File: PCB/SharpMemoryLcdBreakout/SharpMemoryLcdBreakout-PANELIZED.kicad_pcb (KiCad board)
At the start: 2 copper layers, 62 x 42 mm, 49 parts, among them J1 Pin Header, J2 EMD, J3 FH12-10S-0.5SH

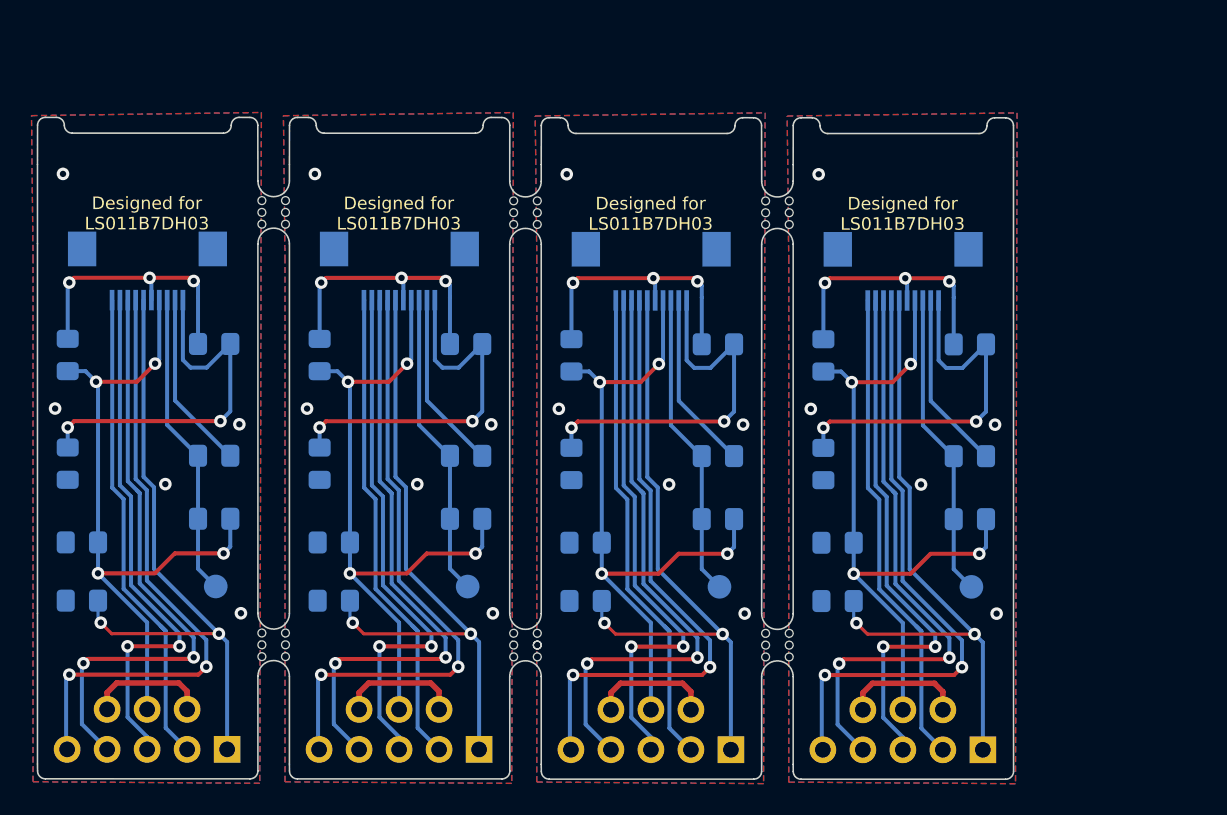
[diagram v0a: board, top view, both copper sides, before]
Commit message: going back to 0603 for easier part selection
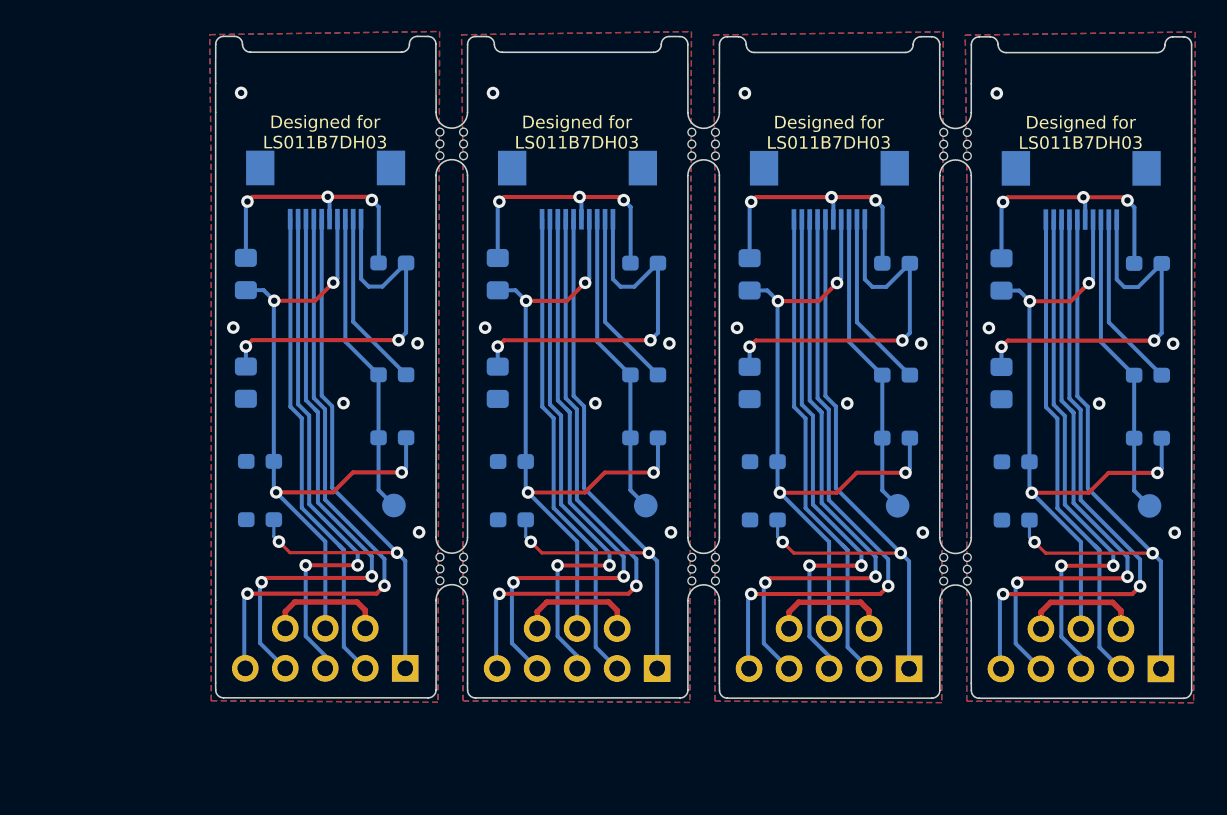
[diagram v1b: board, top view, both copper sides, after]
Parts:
- removed ? (x3): , 
- removed the C1 at (89.4, 67.3)
- removed the C1 at (73.4, 67.3)
- removed the C1 at (57.4, 67.3)
- removed the C2 at (81.8, 51.0)
- removed the C2 at (97.8, 51.0)
- removed the C2 at (65.8, 51.0)
- removed the C3 at (89.4, 63.6)
- removed the C3 at (57.4, 63.6)
- removed the C3 at (73.4, 63.6)
- removed the FB1 at (56.5, 51.7)
- removed the FB1 at (72.5, 51.7)
- removed the FB1 at (88.5, 51.7)
- removed the FB2 at (72.5, 58.6)
- removed the FB2 at (56.5, 58.6)
- removed the FB2 at (88.5, 58.6)
- removed the J1 at (82.6, 76.7)
- removed the J1 at (98.6, 76.7)
- removed the J1 at (66.6, 76.7)
- removed the J2 at (81.9, 66.4)
- removed the J2 at (65.9, 66.4)
- removed the J2 at (97.9, 66.4)
- removed the J3 at (93.6, 46.4)
- removed the J3 at (61.6, 46.3)
- removed the J3 at (77.6, 46.3)
- removed the R1 at (97.8, 58.1)
- removed the R1 at (65.8, 58.1)
- removed the R1 at (81.8, 58.1)
- removed the R2 at (81.8, 62.1)
- removed the R2 at (65.8, 62.1)
- removed the R2 at (97.8, 62.1)
- removed the mouse-bite-2mm-slot at (85.6, 70.1)
- removed the mouse-bite-2mm-slot at (85.6, 42.6)
- removed the mouse-bite-2mm-slot at (69.6, 42.6)
- removed the mouse-bite-2mm-slot at (101.6, 70.1)
- removed the mouse-bite-2mm-slot at (69.6, 70.1)
- removed the mouse-bite-2mm-slot at (101.6, 42.6)
- added C1: 560pF/680pF, Capacitor_SMD:C_0603_1608Metric_Pad1.05x0.95mm_HandSolder, B.Cu at (68.7, 62.1)
- added C1: 560pF/680pF, Capacitor_SMD:C_0603_1608Metric_Pad1.05x0.95mm_HandSolder, B.Cu at (100.7, 62.2)
- added C1: 560pF/680pF, Capacitor_SMD:C_0603_1608Metric_Pad1.05x0.95mm_HandSolder, B.Cu at (84.7, 62.1)
- added C2: 1uF, Capacitor_SMD:C_0603_1608Metric_Pad1.05x0.95mm_HandSolder, B.Cu at (93.1, 45.8)
- added C2: 1uF, Capacitor_SMD:C_0603_1608Metric_Pad1.05x0.95mm_HandSolder, B.Cu at (109.1, 45.9)
- added C2: 1uF, Capacitor_SMD:C_0603_1608Metric_Pad1.05x0.95mm_HandSolder, B.Cu at (77.1, 45.8)
- added C3: 1uF, Capacitor_SMD:C_0603_1608Metric_Pad1.05x0.95mm_HandSolder, B.Cu at (68.7, 58.4)
- added C3: 1uF, Capacitor_SMD:C_0603_1608Metric_Pad1.05x0.95mm_HandSolder, B.Cu at (84.7, 58.4)
- added C3: 1uF, Capacitor_SMD:C_0603_1608Metric_Pad1.05x0.95mm_HandSolder, B.Cu at (100.7, 58.5)
- added FB1: Ferrite_Bead, Resistor_SMD:R_0805_2012Metric_Pad1.15x1.40mm_HandSolder, B.Cu at (99.8, 46.6)
- added FB1: Ferrite_Bead, Resistor_SMD:R_0805_2012Metric_Pad1.15x1.40mm_HandSolder, B.Cu at (83.8, 46.5)
- added FB1: Ferrite_Bead, Resistor_SMD:R_0805_2012Metric_Pad1.15x1.40mm_HandSolder, B.Cu at (67.8, 46.5)
- added FB2: Ferrite_Bead, Resistor_SMD:R_0805_2012Metric_Pad1.15x1.40mm_HandSolder, B.Cu at (83.8, 53.4)
- added FB2: Ferrite_Bead, Resistor_SMD:R_0805_2012Metric_Pad1.15x1.40mm_HandSolder, B.Cu at (67.8, 53.4)
- added FB2: Ferrite_Bead, Resistor_SMD:R_0805_2012Metric_Pad1.15x1.40mm_HandSolder, B.Cu at (99.8, 53.5)
- added J1: Pin Header, SharpMemoryLcdBreakout:PinSocket_2Row_5+3_P2.54mm_Vertical, F.Cu at (93.9, 71.6)
- added J1: Pin Header, SharpMemoryLcdBreakout:PinSocket_2Row_5+3_P2.54mm_Vertical, F.Cu at (78.0, 71.6)
- added J1: Pin Header, SharpMemoryLcdBreakout:PinSocket_2Row_5+3_P2.54mm_Vertical, F.Cu at (109.9, 71.6)
- added J2: EMD, TestPoint:TestPoint_Pad_D1.5mm, B.Cu at (77.2, 61.2)
- added J2: EMD, TestPoint:TestPoint_Pad_D1.5mm, B.Cu at (93.2, 61.2)
- added J2: EMD, TestPoint:TestPoint_Pad_D1.5mm, B.Cu at (109.2, 61.3)
- added J3: FH12-10S-0.5SH, Connector_FFC-FPC:Hirose_FH12-10S-0.5SH_1x10-1MP_P0.50mm_Horizontal, B.Cu at (104.9, 41.2)
- added J3: FH12-10S-0.5SH, Connector_FFC-FPC:Hirose_FH12-10S-0.5SH_1x10-1MP_P0.50mm_Horizontal, B.Cu at (88.9, 41.2)
- added J3: FH12-10S-0.5SH, Connector_FFC-FPC:Hirose_FH12-10S-0.5SH_1x10-1MP_P0.50mm_Horizontal, B.Cu at (72.9, 41.2)
- added R1: 10kΩ, Resistor_SMD:R_0603_1608Metric_Pad1.05x0.95mm_HandSolder, B.Cu at (93.1, 52.9)
- added R1: 10kΩ, Resistor_SMD:R_0603_1608Metric_Pad1.05x0.95mm_HandSolder, B.Cu at (109.1, 53.0)
- added R1: 10kΩ, Resistor_SMD:R_0603_1608Metric_Pad1.05x0.95mm_HandSolder, B.Cu at (77.1, 52.9)
- added R2: 10kΩ, Resistor_SMD:R_0603_1608Metric_Pad1.05x0.95mm_HandSolder, B.Cu at (109.1, 57.0)
- added R2: 10kΩ, Resistor_SMD:R_0603_1608Metric_Pad1.05x0.95mm_HandSolder, B.Cu at (93.1, 56.9)
- added R2: 10kΩ, Resistor_SMD:R_0603_1608Metric_Pad1.05x0.95mm_HandSolder, B.Cu at (77.1, 56.9)
- added mouse-bite-2mm-slot: VAL**, SharpMemoryLcdBreakout:mouse-bite-2mm-slot, F.Cu at (112.9, 65.3)
- added mouse-bite-2mm-slot: VAL**, SharpMemoryLcdBreakout:mouse-bite-2mm-slot, F.Cu at (112.9, 38.3)
- added mouse-bite-2mm-slot: VAL**, SharpMemoryLcdBreakout:mouse-bite-2mm-slot, F.Cu at (96.9, 38.3)
- added mouse-bite-2mm-slot: VAL**, SharpMemoryLcdBreakout:mouse-bite-2mm-slot, F.Cu at (80.9, 65.3)
- added mouse-bite-2mm-slot: VAL**, SharpMemoryLcdBreakout:mouse-bite-2mm-slot, F.Cu at (80.9, 38.3)
- added mouse-bite-2mm-slot: VAL**, SharpMemoryLcdBreakout:mouse-bite-2mm-slot, F.Cu at (96.9, 65.3)
- C1: value 560pF -> 560pF/680pF; footprint Capacitor_SMD:C_0805_2012Metric_Pad1.15x1.40mm_HandSolder -> Capacitor_SMD:C_0603_1608Metric_Pad1.05x0.95mm_HandSolder
- C2, C3: footprint Capacitor_SMD:C_0805_2012Metric_Pad1.15x1.40mm_HandSolder -> Capacitor_SMD:C_0603_1608Metric_Pad1.05x0.95mm_HandSolder
- R1, R2: footprint Resistor_SMD:R_0805_2012Metric_Pad1.15x1.40mm_HandSolder -> Resistor_SMD:R_0603_1608Metric_Pad1.05x0.95mm_HandSolder
- moved C2 12.4 mm to (125.1, 45.9)
- moved FB1 12.4 mm to (115.8, 46.6)
- moved FB2 12.4 mm to (115.8, 53.5)
- moved J1 12.4 mm to (125.9, 71.6)
- moved J3 12.4 mm to (120.9, 41.2)
- moved R1 12.4 mm to (125.1, 53.0)
- moved R2 12.4 mm to (125.1, 57.0)
- moved J2 12.4 mm to (125.2, 61.3)
- moved C1 12.4 mm to (116.7, 62.2)
- moved C3 12.4 mm to (116.7, 58.5)
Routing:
- net GNDA: track 96.6 -> 94.9 mm
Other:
- outline, holes or cut-outs redrawn
